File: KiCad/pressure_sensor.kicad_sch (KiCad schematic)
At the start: 13 parts, among them IC4 MS5849-30BA, U7 SN74LV1T34DCK, U8 SN74LV1T34DCK, U9 PCA9306

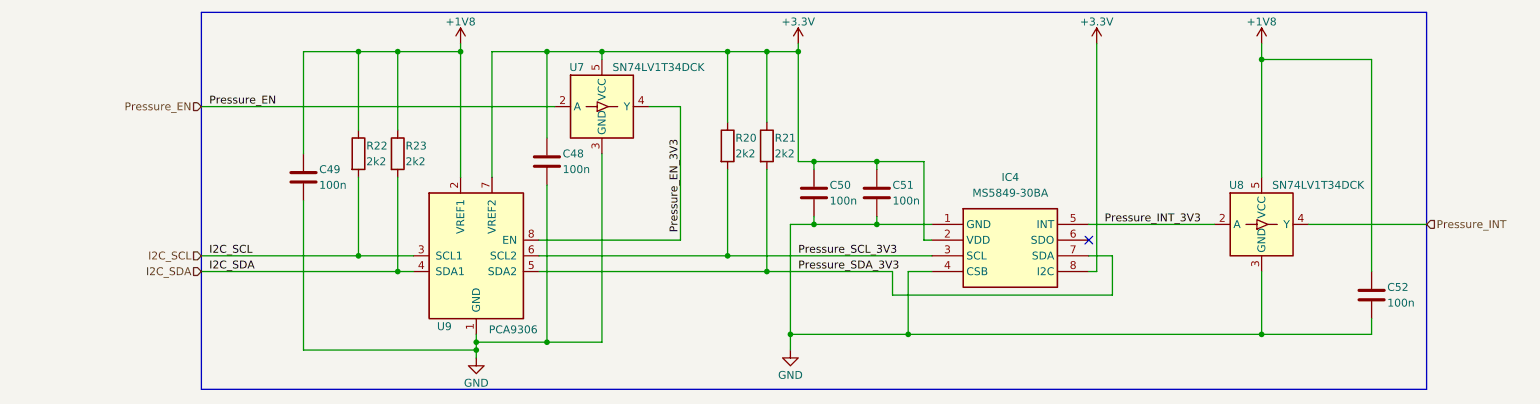
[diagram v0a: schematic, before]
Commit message: V2 beginning with buttons, resistor, ...
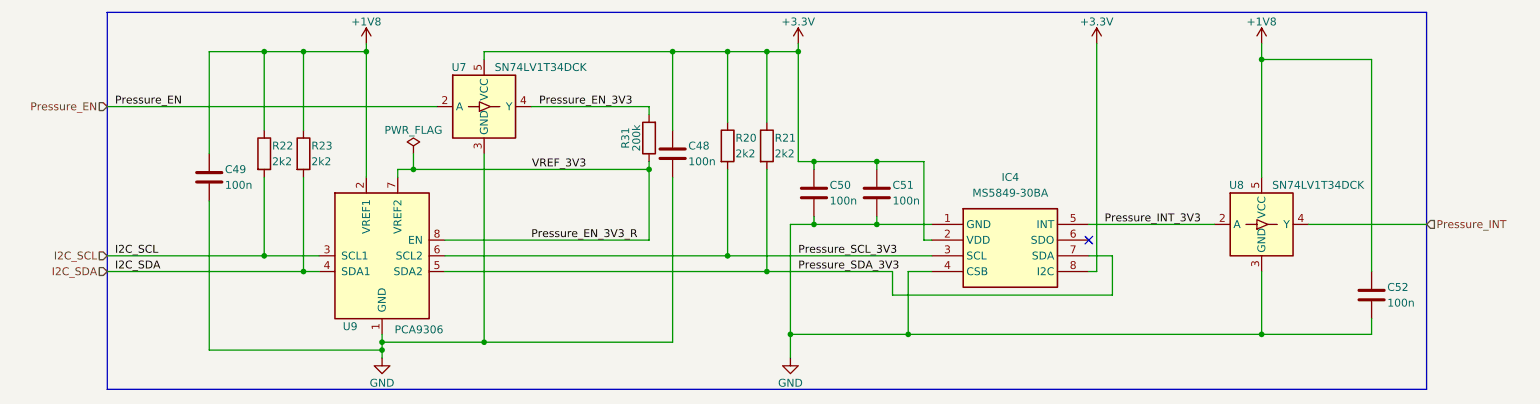
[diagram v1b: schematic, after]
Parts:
- added R31: 200k, Resistor_SMD:R_0402_1005Metric, symbol Device:R
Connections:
- net +3.3V: no longer U9.7 (VREF2)
- net Pressure_EN_3V3: now also R31.2; no longer U9.8 (EN)
- new net Pressure_EN_3V3_R: R31.1, U9.7 (VREF2), U9.8 (EN)
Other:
- moved on the sheet: C48, C49, R22, R23, U7, U9
